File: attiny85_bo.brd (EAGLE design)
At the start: 36 x 20 mm, 11 parts, among them IC1 ATTiny85, J1 AVR_SPI_PRG_6NS, Y1 16MHz

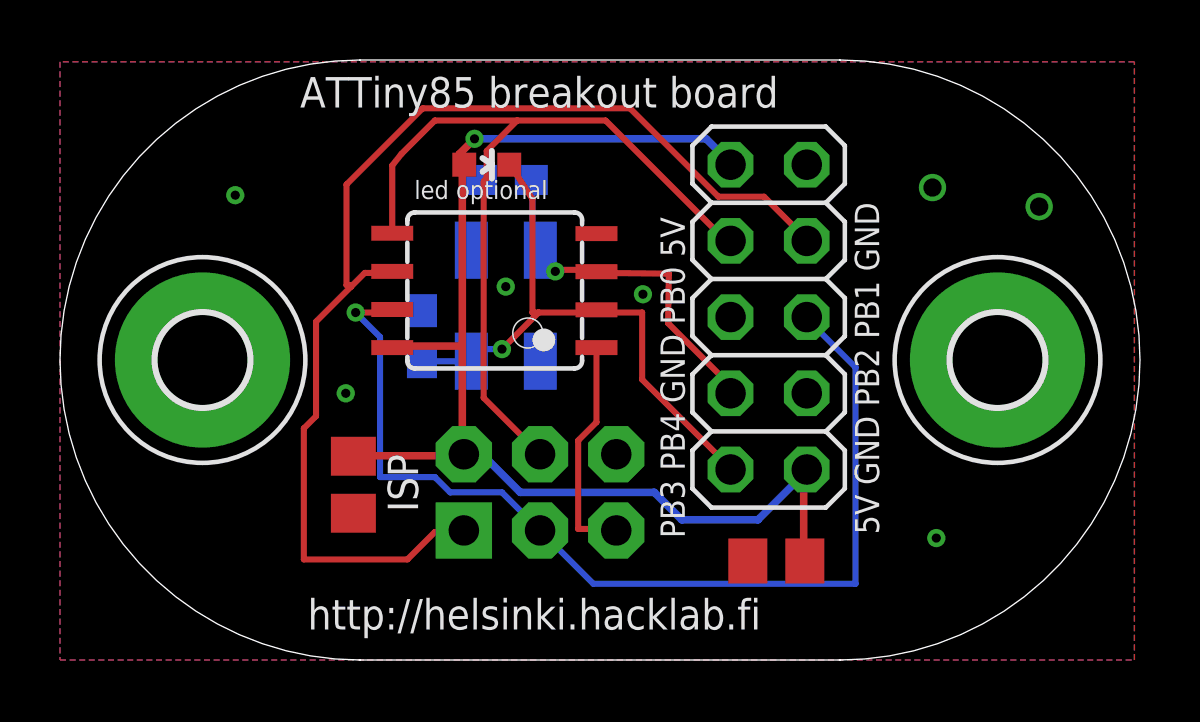
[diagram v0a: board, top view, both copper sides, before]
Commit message: remaking the attiny85 baord so it is more easily connected to stripboard via 90deg pin header
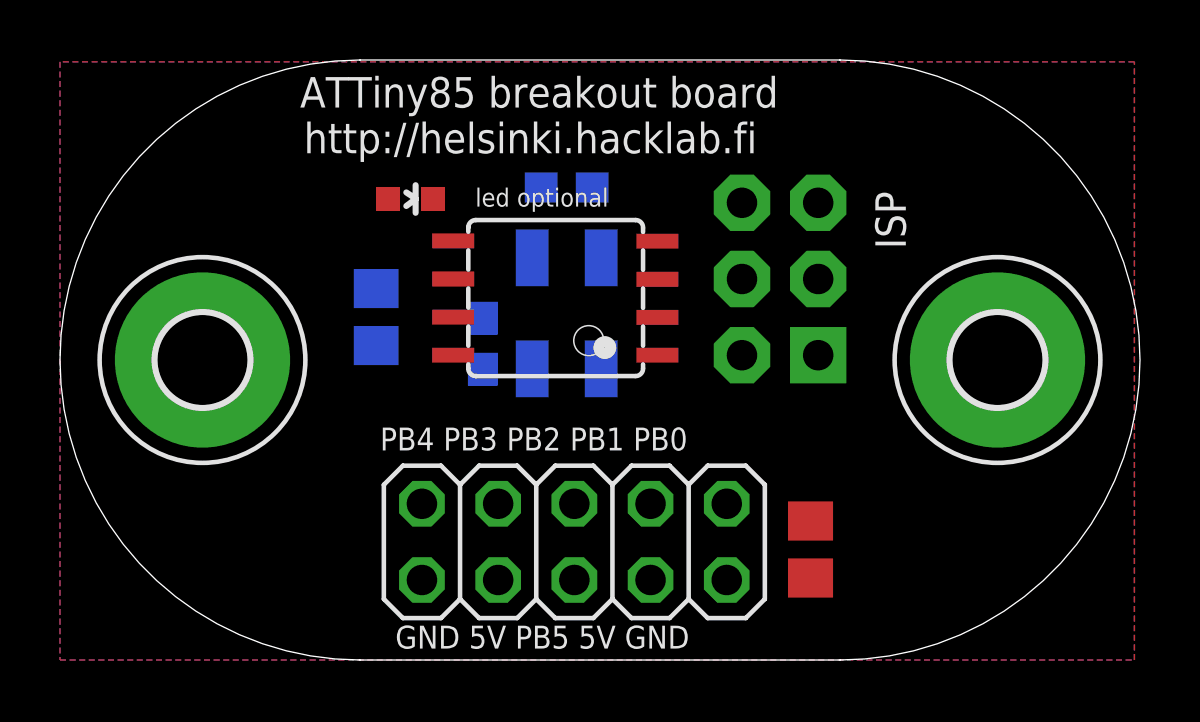
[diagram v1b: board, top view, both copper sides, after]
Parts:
- moved J1 10.7 mm to (24.0, 12.7), turned to 90 degrees
- moved JP1 9.90 mm to (17.1, 3.94), turned to 180 degrees
- moved C1 5.64 mm to (10.5, 11.4), flipped to the bottom, turned to 90 degrees
- moved LED1 2.79 mm to (11.7, 15.4)
- moved IC1 2.05 mm to (16.5, 12.1)
- moved CX1 2.05 mm to (14.1, 10.5)
- moved CX0 2.05 mm to (16.9, 15.7)
- moved Y1 2.05 mm to (16.9, 11.6)
- moved C2 1.20 mm to (25.0, 3.68), turned to 270 degrees
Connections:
- net +5V: now also JP1.4, JP1.8; no longer JP1.1, JP1.10
- net GND: now also JP1.10; no longer JP1.5, JP1.8
- net PB0: now also JP1.1; no longer JP1.3
- net PB1: now also JP1.3; no longer JP1.4
- net PB2: now also JP1.5; no longer JP1.6
- net PB3: now also JP1.7; no longer JP1.9
- net PB4: now also JP1.9; no longer JP1.7
- net PB5: now also JP1.6
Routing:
- net +5V: track 42.1 -> 0.00 mm, vias 1 -> 0
- net PB1: track 38.8 -> 0.00 mm
- net PB2: track 34.0 -> 0.00 mm, vias 1 -> 0
- net PB0: track 28.2 -> 0.00 mm
- net PB3: track 20.0 -> 0.00 mm, vias 1 -> 0
- net PB4: track 12.7 -> 0.00 mm, vias 1 -> 0
- net PB5: track 7.59 -> 0.00 mm
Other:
- board text added: "GND 5V PB5 5V GND"
- board text added: "PB0 PB1 PB2 PB3 PB4"
- board text added: "PB4 PB3 PB2 PB1 PB0"
- board text removed: "5V GND PB2 PB1 GND"
- board text removed: "PB3 PB4 GND PB0 5V"
- board text removed: "on top: bypass caps 2-10uF"

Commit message: route the crystals manually
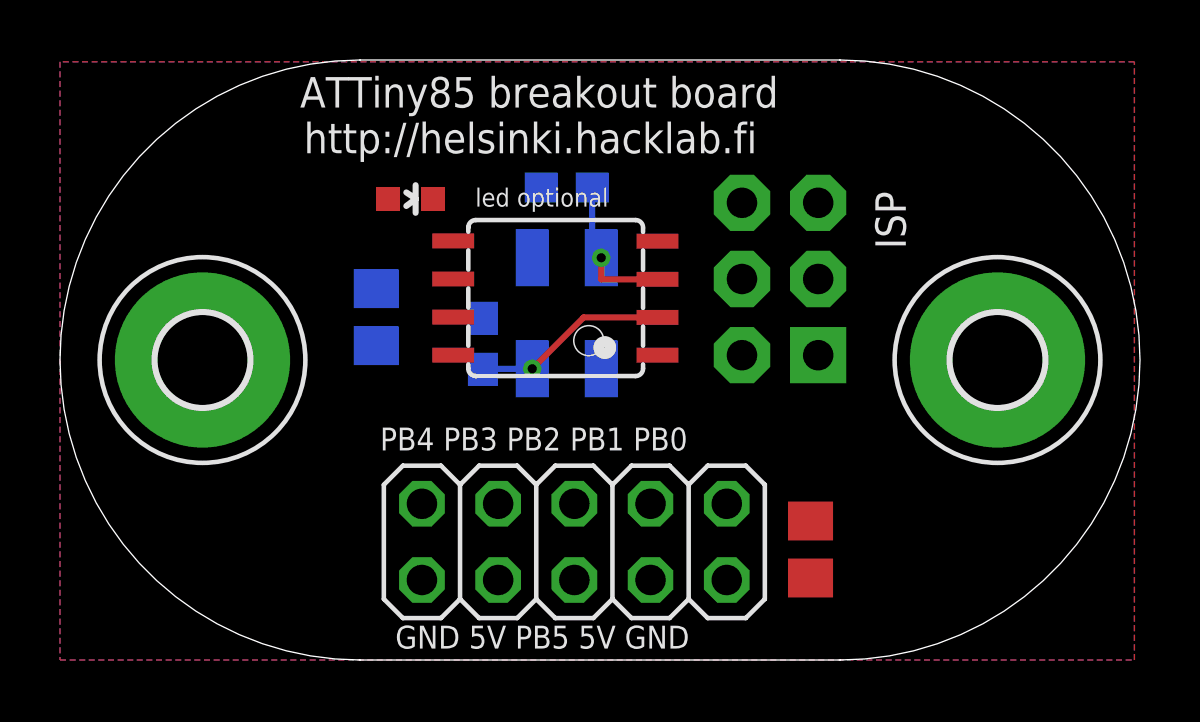
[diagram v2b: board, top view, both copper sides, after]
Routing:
- net PB3: track 0.00 -> 6.53 mm, vias 0 -> 1
- net PB4: track 0.00 -> 5.23 mm, vias 0 -> 1
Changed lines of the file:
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@@
 <contactref element="Y1" pad="1"/>
 <contactref element="JP1" pad="7"/>
-<wire x1="15.741" y1="9.707" x2="19.914" y2="11.42" width="0" layer="19" extent="1-16"/>
-<wire x1="14.097" y1="9.691" x2="15.741" y2="9.707" width="0" layer="19" extent="16-16"/>
-<wire x1="14.605" y1="5.207" x2="14.097" y2="9.691" width="0" layer="19" extent="16-16"/>
-<wire x1="12.434" y1="15.367" x2="14.097" y2="9.691" width="0" layer="19" extent="1-16"/>
+<wire x1="19.914" y1="11.42" x2="17.454" y2="11.42" width="0.2032" layer="1"/>
+<wire x1="17.454" y1="11.42" x2="15.741" y2="9.707" width="0.2032" layer="1"/>
+<via x="15.741" y="9.707" extent="1-16" drill="0.3048"/>
+<wire x1="15.741" y1="9.707" x2="14.113" y2="9.707" width="0.2032" layer="16"/>
+<wire x1="14.113" y1="9.707" x2="14.097" y2="9.691" width="0.2032" layer="16"/>
+<wire x1="14.113" y1="9.707" x2="12.434" y2="15.367" width="0" layer="19" extent="1-16"/>
+<wire x1="14.605" y1="5.207" x2="14.113" y2="9.707" width="0" layer="19" extent="16-16"/>
 </signal>
 <signal name="PB4">
@@
 <contactref element="Y1" pad="3"/>
 <contactref element="JP1" pad="9"/>
-<wire x1="18.041" y1="13.407" x2="17.741" y2="15.748" width="0" layer="19" extent="16-16"/>
-<wire x1="19.914" y1="12.69" x2="18.041" y2="13.407" width="0" layer="19" extent="1-16"/>
-<wire x1="12.065" y1="5.207" x2="18.041" y2="13.407" width="0" layer="19" extent="16-16"/>
+<wire x1="19.914" y1="12.69" x2="18.041" y2="12.69" width="0.2032" layer="1"/>
+<wire x1="18.041" y1="12.69" x2="18.041" y2="13.407" width="0.2032" layer="1"/>
+<via x="18.041" y="13.407" extent="1-16" drill="0.3048"/>
+<wire x1="18.041" y1="13.407" x2="17.741" y2="13.407" width="0.2032" layer="16"/>
+<wire x1="17.741" y1="13.407" x2="17.741" y2="15.748" width="0.2032" layer="16"/>
+<wire x1="12.065" y1="5.207" x2="18.041" y2="12.69" width="0" layer="19" extent="1-1"/>
 </signal>
 </signals>

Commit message: let autorouter take care of the rest
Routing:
- net +5V: track 0.00 -> 38.4 mm, vias 0 -> 2
- net PB0: track 0.00 -> 32.1 mm, vias 0 -> 1
- net PB1: track 0.00 -> 23.9 mm
- net PB2: track 0.00 -> 19.6 mm, vias 0 -> 2
- net PB5: track 0.00 -> 18.0 mm, vias 0 -> 1
- net PB3: track 6.53 -> 18.5 mm
- net PB4: track 5.23 -> 17.2 mm
